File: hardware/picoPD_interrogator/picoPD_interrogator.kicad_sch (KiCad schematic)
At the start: 50 parts, among them Q1 rohm-RE1C002UN, Q2 rohm-RE1C002UN, Q3 rohm-RE1C002UN, Q4 rohm-RE1C002UN, Q5 rohm-RE1C002UN, U2 ST-LM393QT, U7 LV2862XDDC

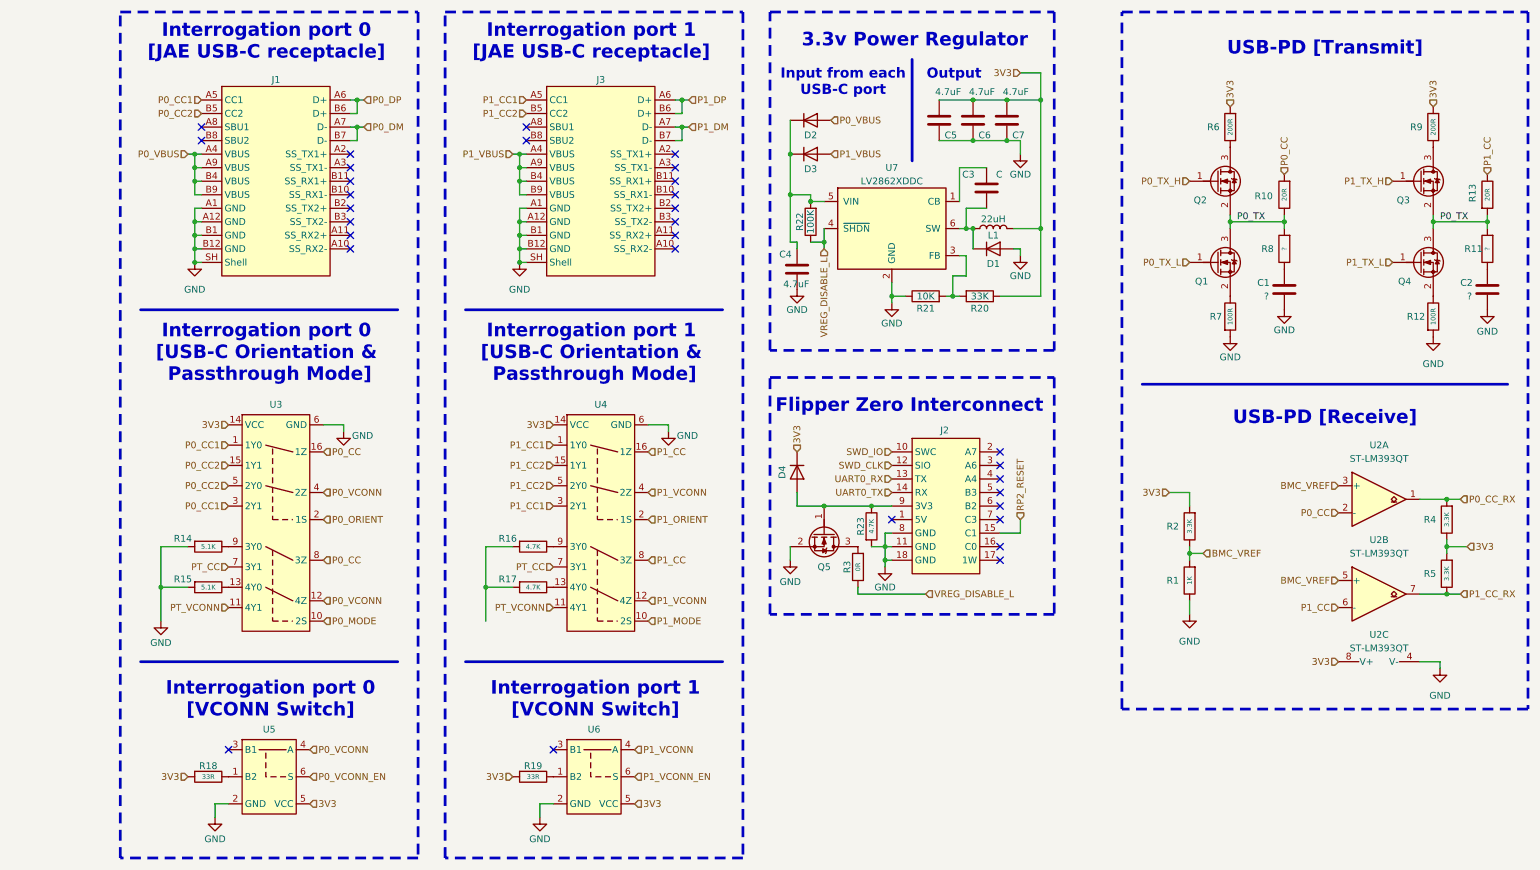
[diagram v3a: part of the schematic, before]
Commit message: Schematic: Moved USB-PD stuff to a seperate page for space purposes. Also created a page for the RP2 components.
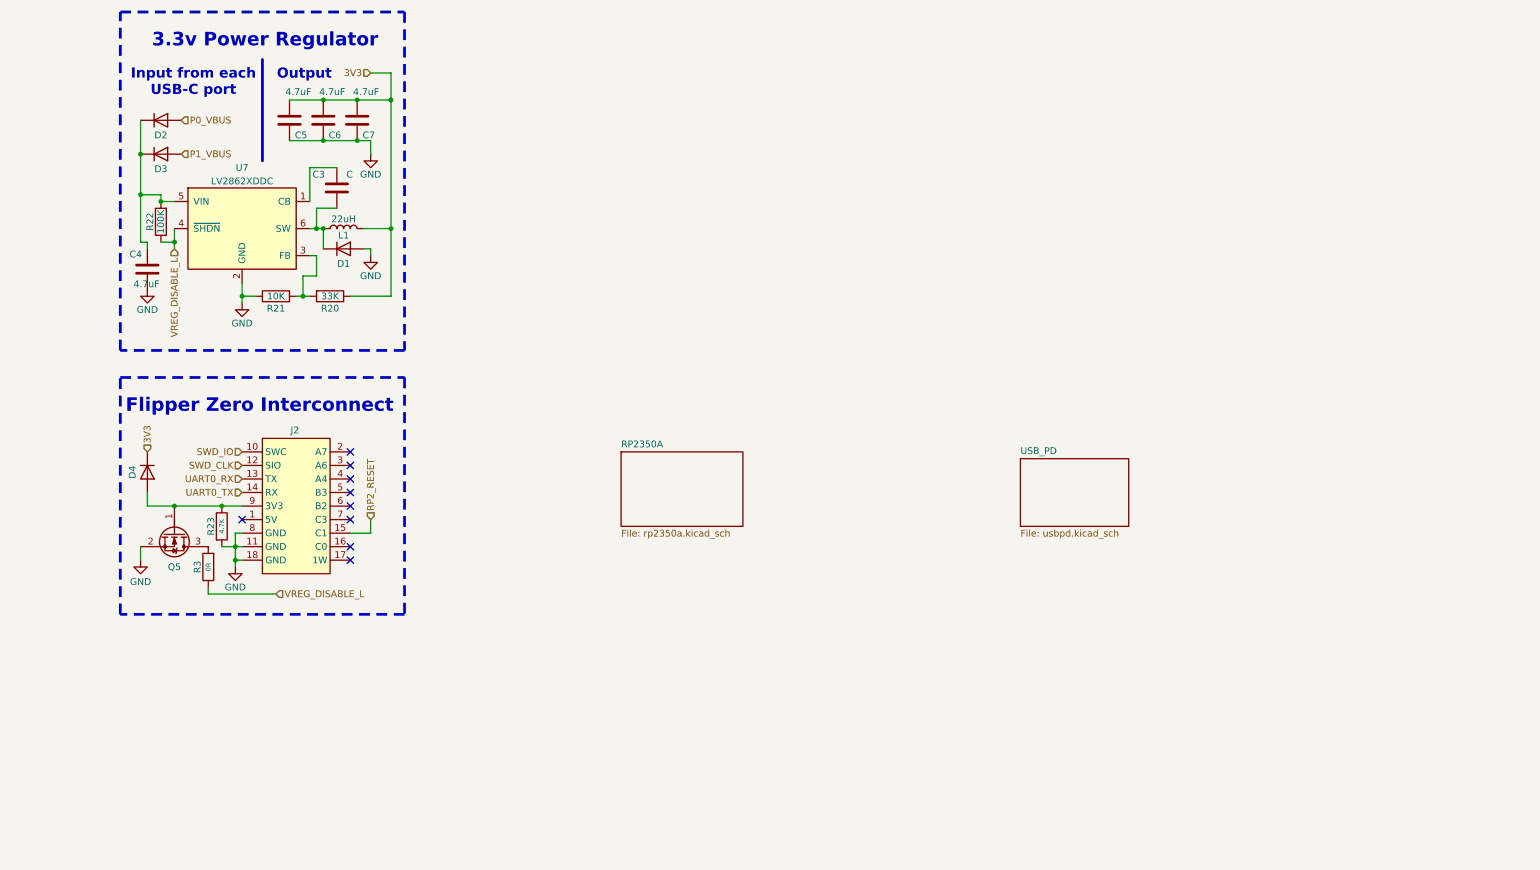
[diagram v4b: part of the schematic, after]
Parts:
- removed C1, C2: ?, Capacitor_SMD:C_0201_0603Metric, symbol Device:C
- removed J1, J3: ~, picoPD_interrogator:JAE_DX07BN24JA2R1300, symbol picoPD_interrogator:USB-C_24pSH
- removed Q1, Q2, Q3, Q4: rohm-RE1C002UN, Package_TO_SOT_SMD:SOT-416, symbol picoPD_interrogator:rohm-RE1C002UN
- removed R1: 1K, Resistor_SMD:R_0201_0603Metric, symbol Device:R
- removed R10, R13: 20R, Resistor_SMD:R_0201_0603Metric, symbol Device:R
- removed R11, R8: ?, Resistor_SMD:R_0201_0603Metric, symbol Device:R
- removed R12, R7: 100R, Resistor_SMD:R_0201_0603Metric, symbol Device:R
- removed R14, R15: 5.1K, Resistor_SMD:R_0201_0603Metric, symbol Device:R
- removed R16, R17: 4.7K, Resistor_SMD:R_0201_0603Metric, symbol Device:R
- removed R18, R19: 33R, Resistor_SMD:R_0201_0603Metric, symbol Device:R
- removed R2, R4, R5: 3.3K, Resistor_SMD:R_0201_0603Metric, symbol Device:R
- removed R6, R9: 200R, Resistor_SMD:R_0201_0603Metric, symbol Device:R
- removed U2: ST-LM393QT, picoPD_interrogator:DFN-8_2x2mm_P0.5mm_ST, symbol picoPD_interrogator:ST-LM393QT
- removed U3, U4: ~, picoPD_interrogator:NXP_NX3DV3899GU, symbol picoPD_interrogator:NXP_NX3DV3899GU
- removed U5, U6: ~, picoPD_interrogator:TI_sn741vc1g3157-q1, symbol picoPD_interrogator:TI_sn741vc1g3157-q1
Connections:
- no-connect marks 52 -> 30
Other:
- added sheet RP2350A (rp2350a.kicad_sch)
- added sheet USB_PD (usbpd.kicad_sch)
- note removed: "Interrogation port 0 [JAE USB-C receptacle]"
- note removed: "Interrogation port 0 [USB-C Orientation & Passthrough Mode]"
- note removed: "Interrogation port 0 [VCONN Switch]"
- note removed: "Interrogation port 1 [JAE USB-C receptacle]"
- note removed: "Interrogation port 1 [USB-C Orientation & Passthrough Mode]"
- note removed: "Interrogation port 1 [VCONN Switch]"
- note removed: "USB-PD [Receive]"
- note removed: "USB-PD [Transmit]"
- moved on the sheet: C3, C4, C5, C6, C7, D1, D2, D3, D4, J2, L1, Q5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

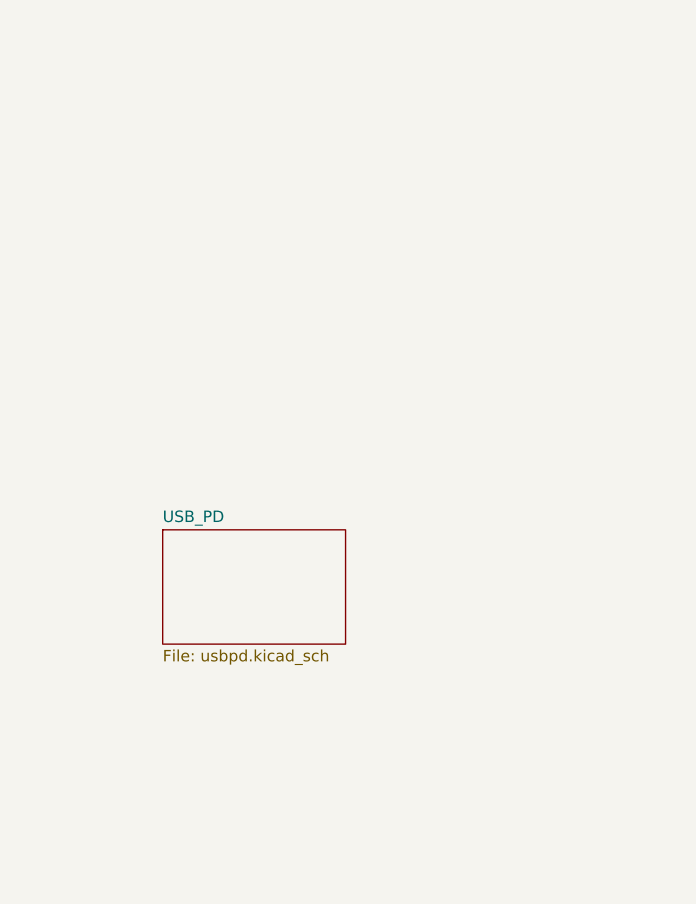
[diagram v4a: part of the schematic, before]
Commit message: Schematic: Imported USB-PD hierarchical labels to the main page.
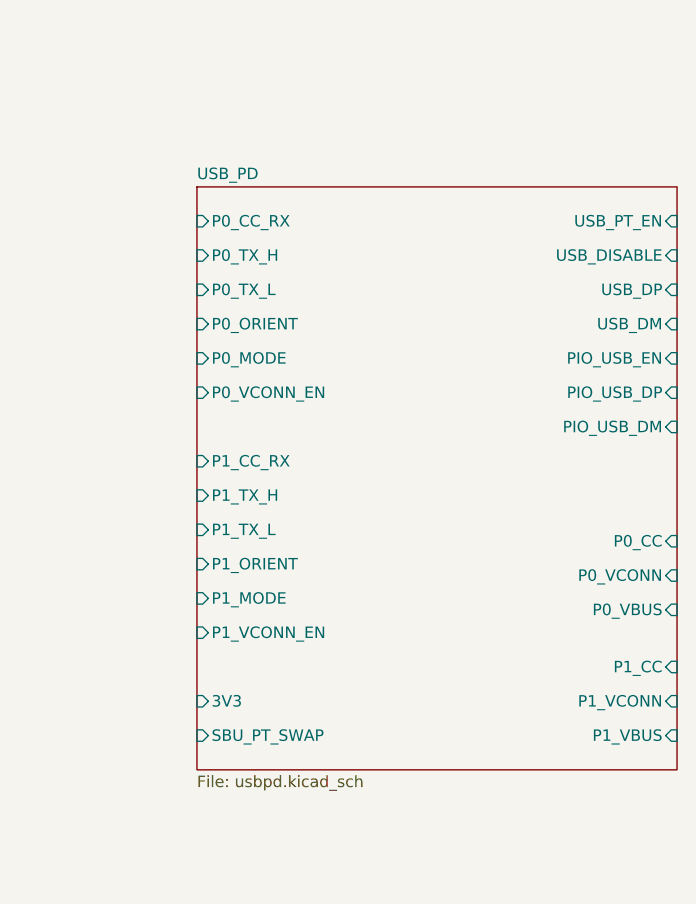
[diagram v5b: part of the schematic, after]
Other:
- sheet USB_PD ports: added 3V3, P0_CC, P0_CC_RX, P0_MODE, P0_ORIENT, P0_TX_H, P0_TX_L, P0_VBUS, P0_VCONN, P0_VCONN_EN, P1_CC, P1_CC_RX, P1_MODE, P1_ORIENT, P1_TX_H, P1_TX_L, P1_VBUS, P1_VCONN, P1_VCONN_EN, PIO_USB_DM, PIO_USB_DP, PIO_USB_EN, SBU_PT_SWAP, USB_DISABLE, USB_DM, USB_DP, USB_PT_EN; removed none

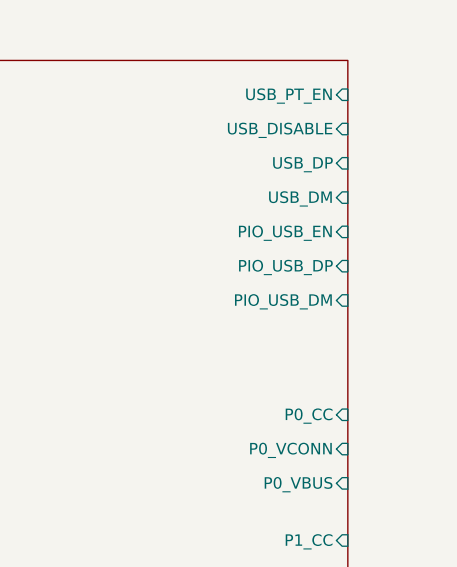
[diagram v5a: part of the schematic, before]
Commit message: Schematic: Added QWIIC Connector. Changed 56K Rp resistor to 35K since we are pulling up 3.3v instead of 5v.
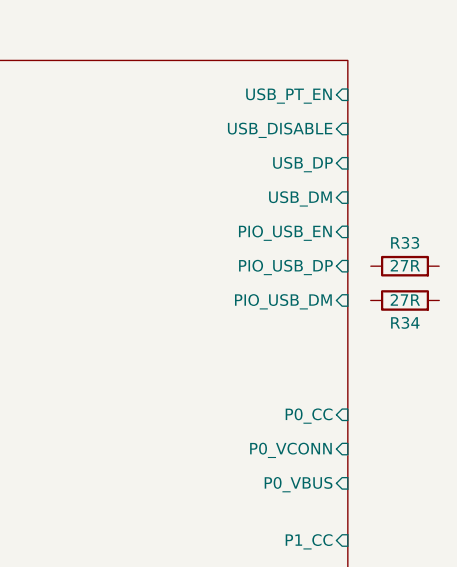
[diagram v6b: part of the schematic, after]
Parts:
- added R33, R34: 27R, symbol Device:R
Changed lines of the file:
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@@
+	)
+	(symbol
+		(lib_name "R_2")
+		(lib_id "Device:R")
+		(at 248.92 85.09 90)
+		(unit 1)
+		(exclude_from_sim no)
+		(in_bom yes)
+		(on_board yes)
+		(dnp no)
+		(property "Reference" "R33"
+			(at 248.92 82.55 90)
+			(effects
+				(font
+					(size 1.27 1.27)
+				)
+			)
+		)
+		(property "Value" "27R"
+			(at 248.92 85.09 90)
+			(effects
+				(font
+					(size 1.27 1.27)
+				)
+			)
+		)
+		(property "Footprint" ""
+			(at 248.92 86.868 90)
+			(effects
+				(font
+					(size 1.27 1.27)
+				)
+				(hide yes)
+			)
+		)
+		(property "Datasheet" "~"
+			(at 248.92 85.09 0)
+			(effects
+				(font
+					(size 1.27 1.27)
+				)
+				(hide yes)
+			)
+		)
+		(property "Description" "Resistor"
+			(at 248.92 85.09 0)
+			(effects
+				(font
+					(size 1.27 1.27)
+				)
+				(hide yes)
+			)
+		)
+		(pin "1"
+		)
+		(pin "2"
+		)
+		(instances
+			(project ""
+				(path "/e34b0978-7def-4921-94d0-accc0a677529"
+					(reference "R33")
+					(unit 1)
+				)
+			)
+		)
 	)
 	(symbol
@@
 					(unit 1)
 				)
+			)
+		)
+	)
+	(symbol
+		(lib_name "R_2")
+		(lib_id "Device:R")
+		(at 248.92 88.9 90)
+		(unit 1)
+		(exclude_from_sim no)
+		(in_bom yes)
+		(on_board yes)
+		(dnp no)
+		(property "Reference" "R34"
+			(at 248.92 91.44 90)
+			(effects
+				(font
+					(size 1.27 1.27)
+				)
+			)
+		)
+		(property "Value" "27R"
+			(at 248.92 88.9 90)
+			(effects
+				(font
+					(size 1.27 1.27)
+				)
+			)
+		)
+		(property "Footprint" ""
+			(at 248.92 90.678 90)
+			(effects
+				(font
+					(size 1.27 1.27)
+				)
+				(hide yes)
+			)
+		)
+		(property "Datasheet" "~"
+			(at 248.92 88.9 0)
+			(effects
+				(font
+					(size 1.27 1.27)
+				)
+				(hide yes)
+			)
+		)
+		(property "Description" "Resistor"
+			(at 248.92 88.9 0)
+			(effects
+				(font
+					(size 1.27 1.27)
+				)
+				(hide yes)
+			)
+		)
+		(pin "1"
+		)
+		(pin "2"
+		)
+		(instances
+			(project "picoPD_interrogator"
+				(path "/e34b0978-7def-4921-94d0-accc0a677529"
+					(reference "R34")
+					(unit 1)
+				)

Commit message: Added RP2350A.
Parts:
- added JP1, JP2, JP3: SolderJumper_2_Bridged, symbol Jumper:SolderJumper_2_Bridged
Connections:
- net P0_VBUS: now also JP1.1 (A)
- net P1_VBUS: now also JP1.2 (B)
- net REG_CAP: now reaches C3.1, U7.1 (CB)
- net REG_FB: now reaches R20.2, R21.2, U7.3 (FB)
- net REG_VIN: now reaches C4.2, D2.1 (K), D3.1 (K), R22.2, U7.5 (VIN)
- net REG_SW: now reaches C3.2, D1.1 (K), L1.1, U7.6 (SW)
- net PIO_USB_DM: now reaches R33.1
- net RP2350A/GP19: now reaches R33.2
- net PIO_USB_DP: now reaches R34.1
- net RP2350A/GP18: now reaches R34.2
- new net P0_VCONN: JP2.1 (A)
- new net P1_VCONN: JP3.1 (A)
- new net RP2350A/GP28_ADC2: JP2.2 (B)
- new net RP2350A/GP29_ADC3: JP3.2 (B)
- no-connect marks 30 -> 32
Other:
- sheet RP2350A ports: added 3V3, GP0, GP1, GP10, GP11, GP12, GP13, GP14, GP15, GP16, GP17, GP18, GP19, GP2, GP20_SDA, GP21_SCL, GP22, GP23, GP24, GP25, GP26_ADC0, GP27_ADC1, GP28_ADC2, GP29_ADC3, GP3, GP4, GP5, GP6, GP7, GP8, GP9, RP2_RESET, SWD_CLK, SWD_IO, USB_DM, USB_DP; removed none
- note added: "Passes VBUS power from Port 0 to Port 1"
- note added: "Raspberry Pi RP2350"
- note added: "This block implements the hardware necessary for a PIO/software-level USB-PD PHY. Unlike many other USB-PD implementations - ALL USB-PD communication must be initiated in software. [Including GoodCRC response frames]"
- note added: "USB-C VBUS Bridge"
- note added: "USB-C ports with Power Delivery Logic & USB Bus Logic"
- moved on the sheet: R33, R34

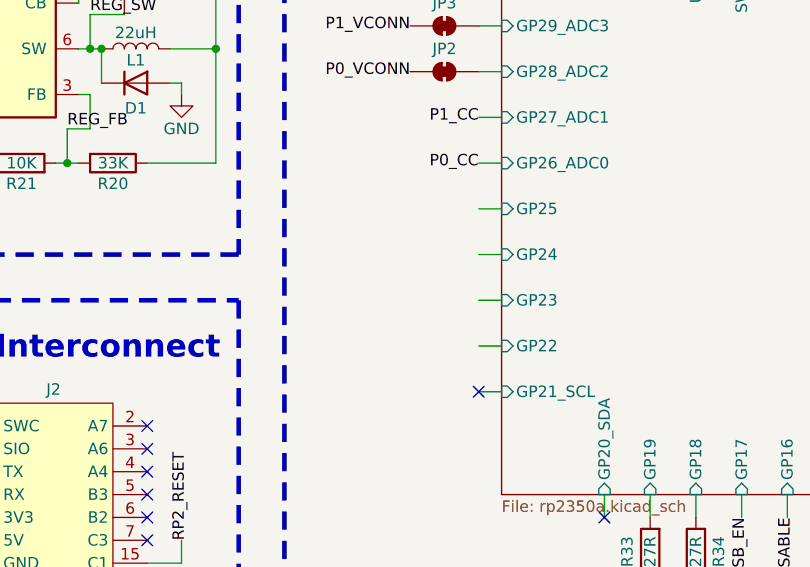
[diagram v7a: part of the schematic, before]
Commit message: Schematic: Added an 'Extra Pins' connector.
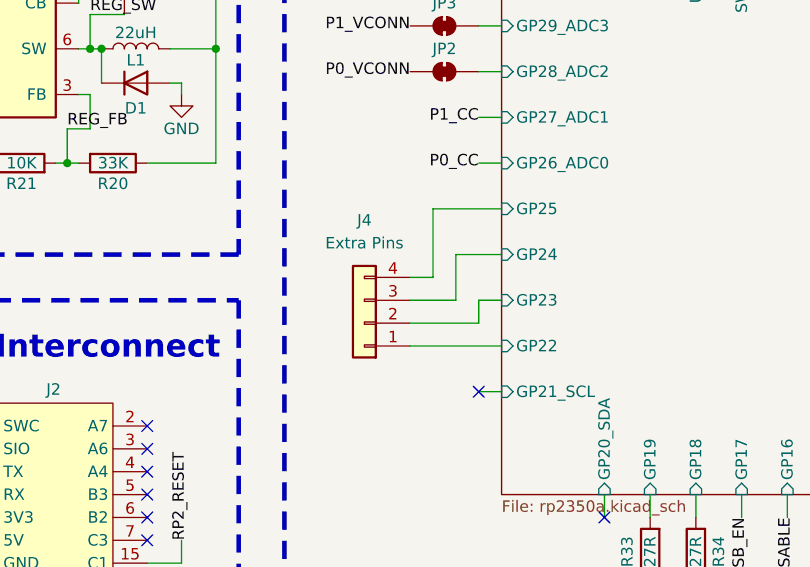
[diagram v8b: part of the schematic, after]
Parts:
- added J4: Extra Pins, Connector_PinHeader_1.00mm:PinHeader_1x04_P1.00mm_Vertical, symbol Connector_Generic:Conn_01x04
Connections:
- net RP2350A/GP22: now also J4.1 (Pin_1)
- net RP2350A/GP23: now also J4.2 (Pin_2)
- net RP2350A/GP24: now also J4.3 (Pin_3)
- net RP2350A/GP25: now also J4.4 (Pin_4)
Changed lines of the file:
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@@
 	(wire
 		(pts
-			(xy 96.52 80.01) (xy 99.06 80.01)
-		)
-		(stroke
-			(width 0)
-			(type default)
-		)
-	)
-	(wire
-		(pts
 			(xy 35.56 109.22) (xy 39.37 109.22)
 		)
@@
 	(wire
 		(pts
+			(xy 88.9 87.63) (xy 96.52 87.63)
+		)
+		(stroke
+			(width 0)
+			(type default)
+		)
+	)
+	(wire
+		(pts
 			(xy 140.97 109.22) (xy 140.97 106.68)
 		)
@@
 	(wire
 		(pts
+			(xy 91.44 82.55) (xy 88.9 82.55)
+		)
+		(stroke
+			(width 0)
+			(type default)
+		)
+	)
+	(wire
+		(pts
 			(xy 62.23 60.96) (xy 63.5 60.96)
 		)
@@
 	(wire
 		(pts
+			(xy 96.52 87.63) (xy 96.52 85.09)
+		)
+		(stroke
+			(width 0)
+			(type default)
+		)
+	)
+	(wire
+		(pts
 			(xy 52.07 57.15) (xy 53.34 57.15)
 		)
@@
 	(wire
 		(pts
-			(xy 26.67 59.69) (xy 26.67 60.96)
+			(xy 91.44 74.93) (xy 99.06 74.93)
 		)
 		(stroke
@@
 	(wire
 		(pts
-			(xy 96.52 74.93) (xy 99.06 74.93)
+			(xy 26.67 59.69) (xy 26.67 60.96)
 		)
 		(stroke
@@
 	(wire
 		(pts
+			(xy 93.98 80.01) (xy 99.06 80.01)
+		)
+		(stroke
+			(width 0)
+			(type default)
+		)
+	)
+	(wire
+		(pts
 			(xy 125.73 109.22) (xy 125.73 106.68)
 		)
@@
 	(wire
 		(pts
+			(xy 88.9 90.17) (xy 99.06 90.17)
+		)
+		(stroke
+			(width 0)
+			(type default)
+		)
+	)
+	(wire
+		(pts
 			(xy 205.74 62.23) (xy 208.28 62.23)
 		)
@@
 	(wire
 		(pts
+			(xy 93.98 80.01) (xy 93.98 85.09)
+		)
+		(stroke
+			(width 0)
+			(type default)
+		)
+	)
+	(wire
+		(pts
+			(xy 91.44 74.93) (xy 91.44 82.55)
+		)
+		(stroke
+			(width 0)
+			(type default)
+		)
+	)
+	(wire
+		(pts
 			(xy 54.61 40.64) (xy 60.96 40.64)
 		)
@@
 	(wire
 		(pts
+			(xy 93.98 85.09) (xy 88.9 85.09)
+		)
+		(stroke
+			(width 0)
+			(type default)
+		)
+	)
+	(wire
+		(pts
 			(xy 26.67 57.15) (xy 26.67 59.69)
 		)
@@
 	(wire
 		(pts
-			(xy 96.52 90.17) (xy 99.06 90.17)
-		)
-		(stroke
-			(width 0)
-			(type default)
-		)
-	)
-	(wire
-		(pts
 			(xy 135.89 109.22) (xy 135.89 106.68)
 		)
@@
 					(unit 1)
 				)
+			)
+		)
+	)
+	(symbol
+		(lib_id "Connector_Generic:Conn_01x04")
+		(at 83.82 87.63 180)
+		(unit 1)
+		(exclude_from_sim no)
+		(in_bom yes)
+		(on_board yes)
+		(dnp no)
+		(fields_autoplaced yes)
+		(property "Reference" "J4"
+			(at 83.82 76.2 0)
+			(effects
+				(font
+					(size 1.27 1.27)
+				)
+			)
+		)
+		(property "Value" "Extra Pins"
+			(at 83.82 78.74 0)
+			(effects
+				(font
+					(size 1.27 1.27)
+				)
+			)
+		)
+		(property "Footprint" "Connector_PinHeader_1.00mm:PinHeader_1x04_P1.00mm_Vertical"
+			(at 83.82 87.63 0)
+			(effects
+				(font
+					(size 1.27 1.27)
+				)
+				(hide yes)
+			)
+		)
+		(property "Datasheet" "~"
+			(at 83.82 87.63 0)
+			(effects
+				(font
+					(size 1.27 1.27)
+				)
+				(hide yes)
+			)
+		)
+		(property "Description" "Generic connector, single row, 01x04, script generated (kicad-library-utils/schlib/autogen/connector/)"
+			(at 83.82 87.63 0)
+			(effects
+				(font
+					(size 1.27 1.27)
+				)
+				(hide yes)
+			)
+		)
+		(pin "4"
+		)
+		(pin "2"
+		)
+		(pin "1"
+		)
+		(pin "3"
+		)
+		(instances
+			(project ""
+				(path "/e34b0978-7def-4921-94d0-accc0a677529"
+					(reference "J4")
+					(unit 1)
+				)
